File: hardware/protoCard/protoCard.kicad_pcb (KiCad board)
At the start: 2 copper layers, 100 x 99.9 mm, 1036 parts, among them J1 6502 Edge, J2 6502 Pinheader

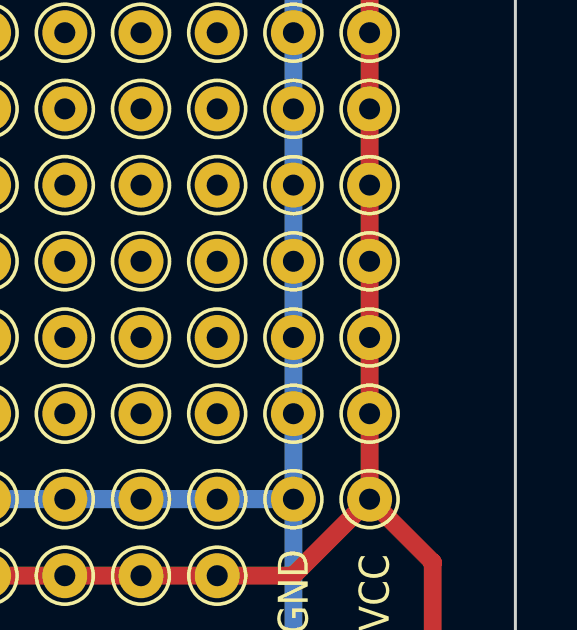
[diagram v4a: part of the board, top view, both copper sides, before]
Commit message: Protoboard Rev 1.2
Fixed pinout of connector and added power led
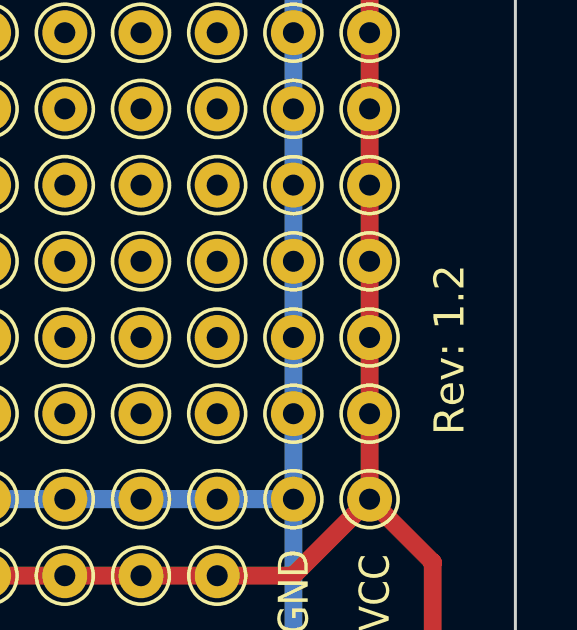
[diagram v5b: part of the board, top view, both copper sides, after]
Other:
- board text added: "Rev: ${REVISION}"
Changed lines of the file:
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@@
   )
   (paper "A4")
+  (title_block
+    (title "6502 ProtoCard")
+    (date "2024-06-26")
+    (rev "1.2")
+  )
   (layers
     (0 "F.Cu" signal)
@@
     (effects (font (size 1 0.6) (thickness 0.15)) (justify left bottom))
   )
+  (gr_text "Rev: ${REVISION}" (at 152.09 98.81 90) (layer "F.SilkS")
+    (effects (font (size 1 1) (thickness 0.15)) (justify left bottom))
+  )
   (gr_text "VCC" (at 55.1 115.45) (layer "F.SilkS")

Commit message: ProtoCard Rev 1.2
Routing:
- net GND: track 422.4 -> 459.4 mm
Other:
- outline, holes or cut-outs redrawn
- board text added: "Simple6502"
- board text added: "Simple6502 ProtoCard"
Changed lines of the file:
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@@
       (disableapertmacros false)
       (usegerberextensions false)
-      (usegerberattributes true)
-      (usegerberadvancedattributes true)
-      (creategerberjobfile true)
+      (usegerberattributes false)
+      (usegerberadvancedattributes false)
+      (creategerberjobfile false)
       (dashed_line_dash_ratio 12.000000)
       (dashed_line_gap_ratio 3.000000)
@@
       (psa4output false)
       (plotreference true)
-      (plotvalue true)
+      (plotvalue false)
       (plotinvisibletext false)
       (sketchpadsonfab false)
-      (subtractmaskfromsilk false)
+      (subtractmaskfromsilk true)
       (outputformat 1)
       (mirror false)
-      (drillshape 1)
+      (drillshape 0)
       (scaleselection 1)
-      (outputdirectory "")
+      (outputdirectory "CAM/")
     )
   )
@@
   (gr_rect (start 53.8 30.5) (end 153.8 130.5)
     (stroke (width 0.15) (type default)) (fill none) (layer "Dwgs.User"))
-  (gr_line (start 53.7 129.2) (end 53.7 30.6)
+  (gr_line (start 53.7 129.2) (end 53.7 34.57)
     (stroke (width 0.1) (type default)) (layer "Edge.Cuts"))
   (gr_line (start 55 130.5) (end 53.7 129.2)
     (stroke (width 0.1) (type default)) (layer "Edge.Cuts"))
-  (gr_line (start 53.7 30.6) (end 153.7 30.6)
+  (gr_line (start 57.67 30.6) (end 152.81 30.6)
+    (stroke (width 0.1) (type default)) (layer "Edge.Cuts"))
+  (gr_arc (start 152.81 30.6) (mid 153.441396 30.865675) (end 153.7 31.5)
     (stroke (width 0.1) (type default)) (layer "Edge.Cuts"))
   (gr_line (start 119.9 129.1) (end 118.5 130.5)
@@
   (gr_line (start 119.9 120.2) (end 153.7 120.2)
     (stroke (width 0.1) (type default)) (layer "Edge.Cuts"))
-  (gr_line (start 153.7 30.6) (end 153.7 120.2)
+  (gr_arc (start 53.7 34.57) (mid 54.862786 31.762787) (end 57.67 30.6)
+    (stroke (width 0.1) (type default)) (layer "Edge.Cuts"))
+  (gr_line (start 153.7 31.5) (end 153.7 120.2)
     (stroke (width 0.1) (type default)) (layer "Edge.Cuts"))
   (gr_line (start 118.5 130.5) (end 55 130.5)
@@
     (effects (font (size 1 0.7) (thickness 0.15)) (justify left bottom))
   )
+  (gr_text "Simple6502" (at 122.14 117.98) (layer "F.SilkS")
+    (effects (font (size 4 3) (thickness 0.5) bold) (justify left bottom))
+  )
   (gr_text "~{IO_05}" (at 109.9 107.95 45) (layer "F.SilkS")
     (effects (font (size 1 0.7) (thickness 0.15)) (justify left bottom))
   )
+  (gr_text "Simple6502 ProtoCard" (at 79.88 32.92) (layer "F.SilkS")
+    (effects (font (size 1.5 1.2) (thickness 0.2) bold) (justify left bottom))
+  )
   (gr_text "A15 A14 A13 A12 A11" (at 68.2 107.45) (layer "F.SilkS")
     (effects (font (size 1 0.7) (thickness 0.15)) (justify left bottom))
@@
     (effects (font (size 1 0.7) (thickness 0.15) bold) (justify left bottom))
   )
-  (gr_text "Protoboard" (at 123.05 117.3) (layer "F.SilkS")
-    (effects (font (size 3 3) (thickness 0.4)) (justify left bottom))
+  (gr_text "Protoboard" (at 122.87 109.54) (layer "F.SilkS")
+    (effects (font (size 3 2.5) (thickness 0.4)) (justify left bottom))
   )
   (gr_text "~{WR}" (at 94.26 107.89 30) (layer "F.SilkS")
@@
   (segment (start 89.34 125.38) (end 89.32 125.4) (width 0.25) (layer "F.Cu") (net 25))
   (segment (start 89.34 112.16) (end 89.34 125.38) (width 0.25) (layer "F.Cu") (net 25))
+  (segment (start 89.34 109.62) (end 89.34 112.16) (width 0.2) (layer "F.Cu") (net 25))
   (segment (start 147.76 108.96) (end 148.445113 108.96) (width 0.6) (layer "F.Cu") (net 25))
   (segment (start 146.3 107.5) (end 141.64 112.16) (width 0.6) (layer "F.Cu") (net 25))
@@
   (segment (start 59.94 37.14) (end 146.3 37.14) (width 0.6) (layer "B.Cu") (net 25))
   (segment (start 92.96 100.95) (end 90.42 100.95) (width 0.6) (layer "B.Cu") (net 25))
+  (segment (start 87.56 107.84) (end 58.1 107.84) (width 0.2) (layer "B.Cu") (net 25))
   (segment (start 89.32 125.4) (end 89.32 114.54) (width 0.2) (layer "B.Cu") (net 25))
   (segment (start 59.94 100.95) (end 146.3 100.95) (width 0.6) (layer "B.Cu") (net 25))
@@
   (segment (start 89.32 114.54) (end 90.6 113.26) (width 0.2) (layer "B.Cu") (net 25))
   (segment (start 56.32 109.62) (end 56.32 104.57) (width 0.6) (layer "B.Cu") (net 25))
+  (segment (start 58.1 107.84) (end 56.32 109.62) (width 0.2) (layer "B.Cu") (net 25))
   (segment (start 54.6 114.5) (end 56.4 116.3) (width 0.6) (layer "B.Cu") (net 25))
   (segment (start 56.4 125.3) (end 56.3 125.4) (width 0.6) (layer "B.Cu") (net 25))
@@
   (segment (start 90.6 110.88) (end 89.34 109.62) (width 0.2) (layer "B.Cu") (net 25))
   (segment (start 56.32 104.57) (end 59.94 100.95) (width 0.6) (layer "B.Cu") (net 25))
+  (segment (start 89.34 109.62) (end 87.56 107.84) (width 0.2) (layer "B.Cu") (net 25))
   (segment (start 90.6 113.26) (end 90.6 110.88) (width 0.2) (layer "B.Cu") (net 25))
   (segment (start 87.88 100.95) (end 90.42 100.95) (width 0.6) (layer "B.Cu") (net 25))
